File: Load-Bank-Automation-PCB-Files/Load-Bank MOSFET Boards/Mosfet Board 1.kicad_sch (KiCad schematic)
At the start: 21 parts, among them J1 Conn_02x03_Counter_Clockwise, J24 PHNX_CONN_1017521, Q22 GSGN0648, Q3 GSGN0648, U10 MCP6006-OTVAO, U7 ACS711xLCTR-25AB, U8 IRS10752LPBF

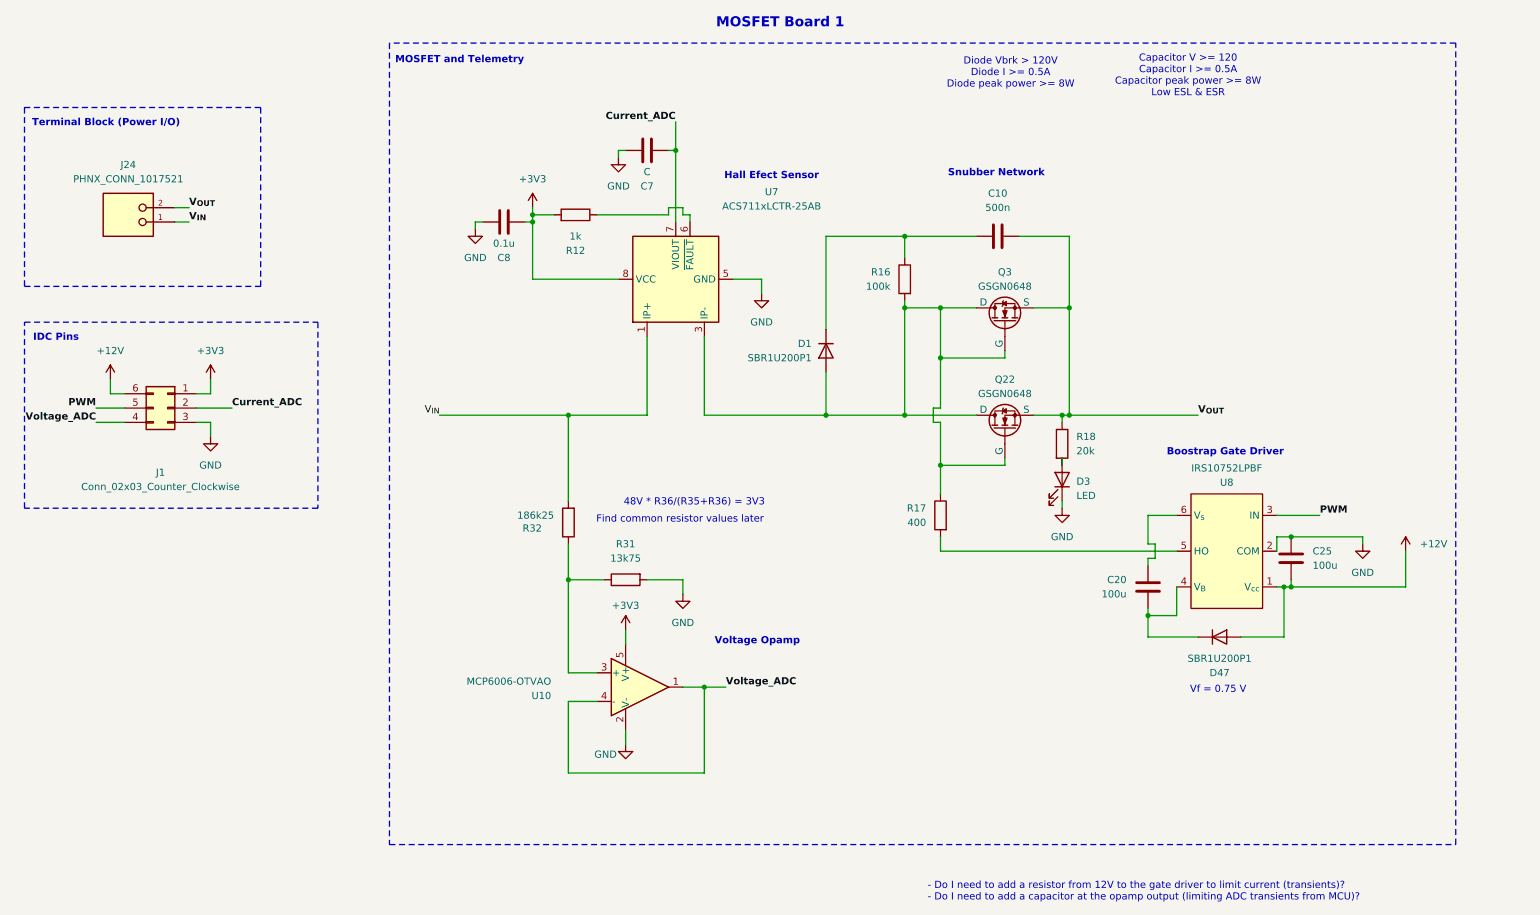
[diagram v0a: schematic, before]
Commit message: Almost completed MOSFET board component selection
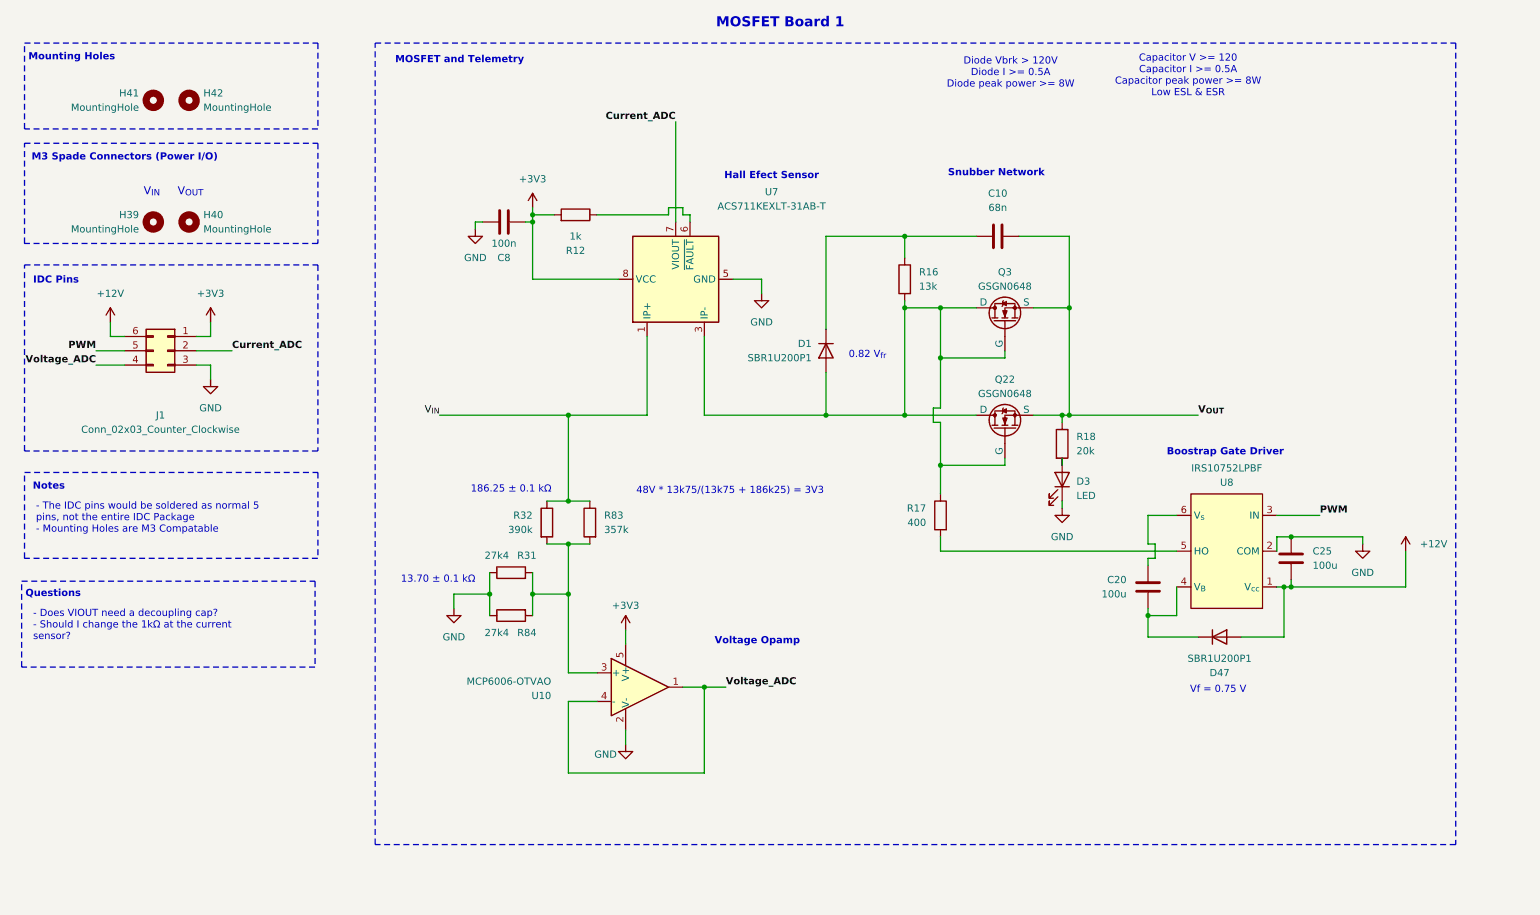
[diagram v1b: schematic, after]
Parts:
- removed C7: C, Capacitor_SMD:C_0603_1608Metric_Pad1.08x0.95mm_HandSolder, symbol Device:C
- removed J24: PHNX_CONN_1017521, ecocad_lib_footprints:PHOENIX_1017521, symbol EcoCar_Library:PHNX_CONN_1017521
- added H39, H40, H41, H42: MountingHole, TerminalBlock_MetzConnect:TerminalBlock_MetzConnect_360271_1x01_Horizontal_ScrewM3.0_Boxed, symbol Mechanical:MountingHole
- added R83: 357k, Resistor_SMD:R_1206_3216Metric_Pad1.30x1.75mm_HandSolder, symbol Device:R
- added R84: 27k4, Resistor_SMD:R_1206_3216Metric_Pad1.30x1.75mm_HandSolder, symbol Device:R
- C10: value 500n -> 68n; footprint (none) -> Capacitor_SMD:C_1206_3216Metric_Pad1.33x1.80mm_HandSolder
- C8: value 0.1u -> 100n
- R16: value 100k -> 13k; footprint (none) -> Resistor_THT:R_Axial_DIN0204_L3.6mm_D1.6mm_P7.62mm_Horizontal
- R31: value 13k75 -> 27k4; footprint (none) -> Resistor_SMD:R_1206_3216Metric_Pad1.30x1.75mm_HandSolder
- R32: value 186k25 -> 390k; footprint (none) -> Resistor_SMD:R_1206_3216Metric_Pad1.30x1.75mm_HandSolder
- U7: value ACS711xLCTR-25AB -> ACS711KEXLT-31AB-T; footprint Package_SO:SOIC-8_3.9x4.9mm_P1.27mm -> Package_DFN_QFN:XDCR_ACS711KEXLT-15AB-T
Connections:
- net GND: now also R31.1, R84.1; no longer R31.2
- net V_{IN}: now also R32.1, R83.1; no longer R32.2
- new net: R31.2, R32.2, R83.2, R84.2, U10.3 (+)
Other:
- note added: "- Does VIOUT need a decoupling cap? - Should I change the 1kΩ at the current sensor?"
- note added: "- The IDC pins would be soldered as normal 5 pins, not the entire IDC Package - Mounting Holes are M3 Compatable"
- note added: "0.82 V_{fr}"
- note added: "13.70 ± 0.1 kΩ"
- note added: "186.25 ± 0.1 kΩ"
- note added: "48V * 13k75/(13k75 + 186k25) = 3V3"
- note added: "M3 Spade Connectors (Power I/O)"
- note added: "Mounting Holes"
- note added: "Notes"
- note added: "Questions"
- note added: "V_{IN}"
- note added: "V_{OUT}"
- note removed: "- Do I need to add a resistor from 12V to the gate driver to limit current (transients)? - Do I need to add a capacitor at the opamp output (limiting ADC transients from MCU)?"
- note removed: "48V * R36/(R35+R36) = 3V3"
- note removed: "Find common resistor values later"
- note removed: "Terminal Block (Power I/O)"
- moved on the sheet: J1

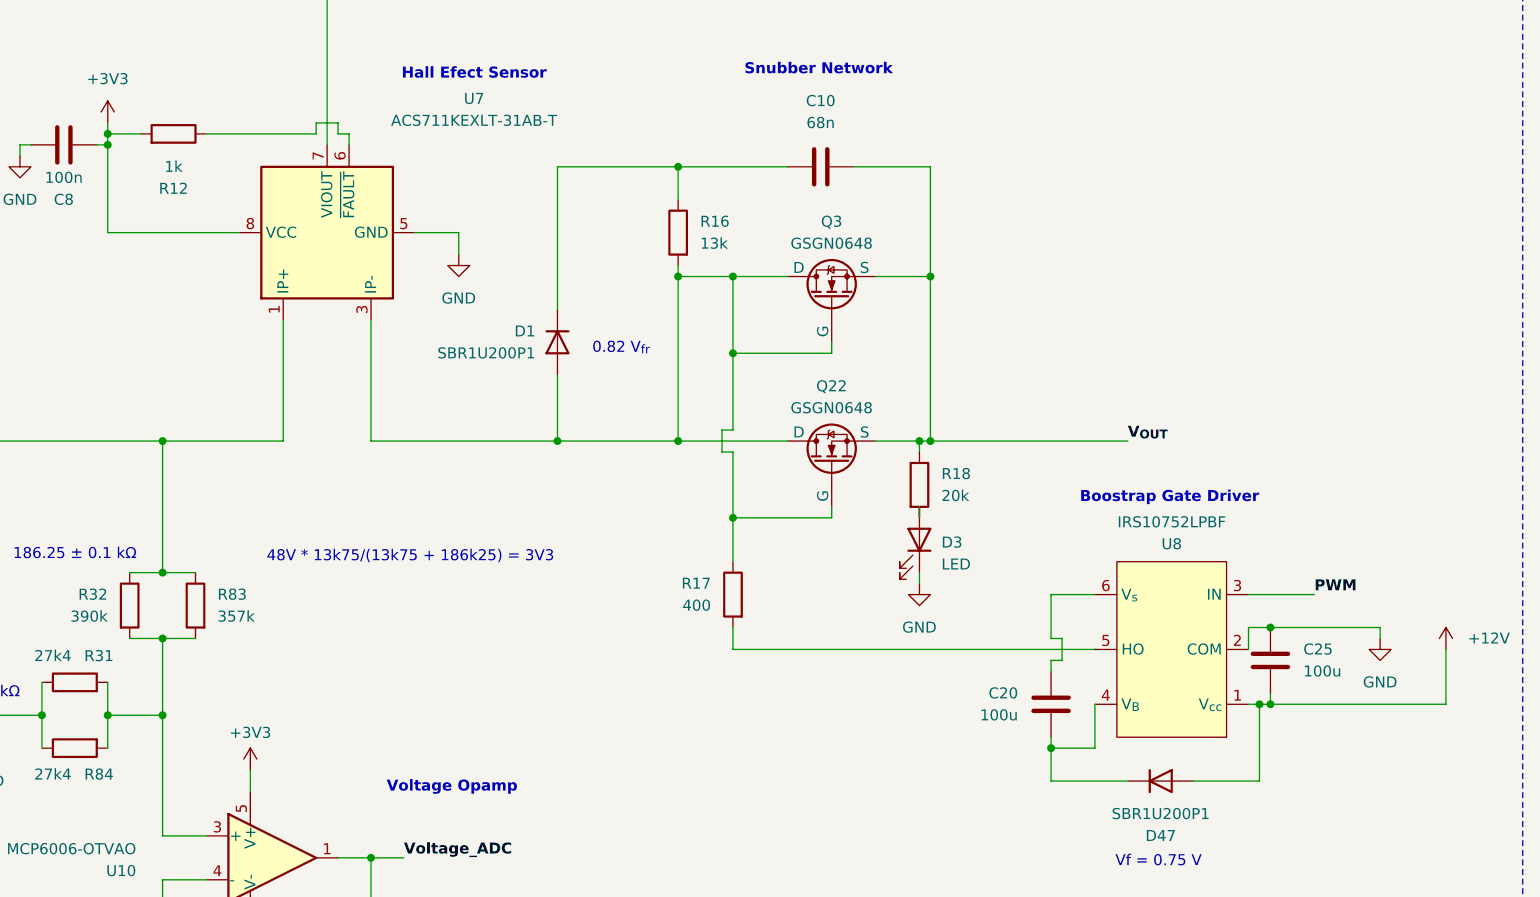
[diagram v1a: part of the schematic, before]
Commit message: All footprints assigned and new schematic changes
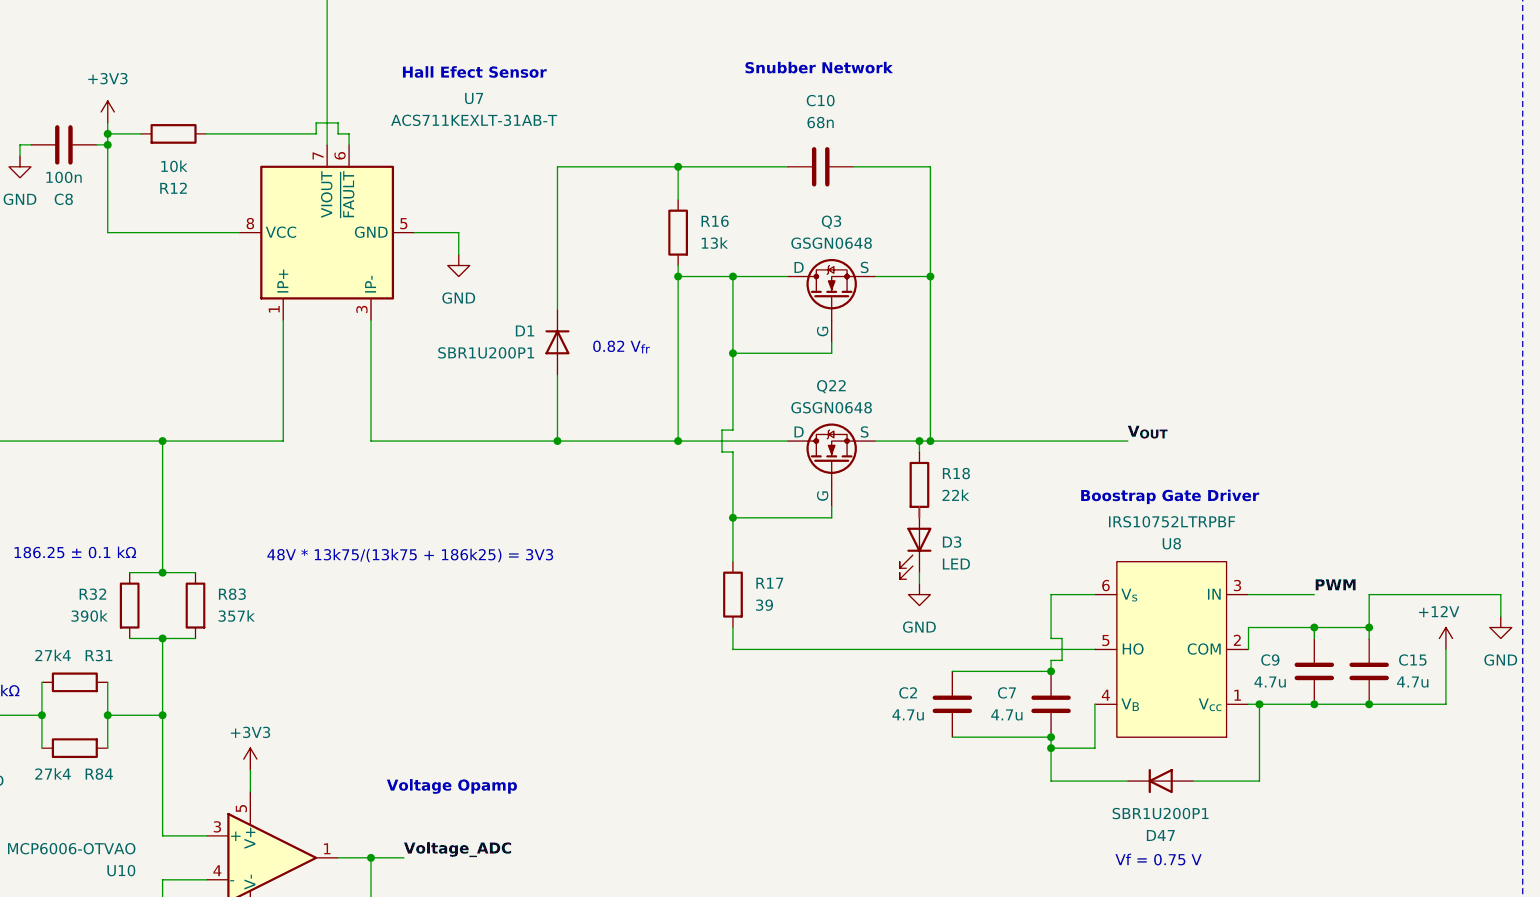
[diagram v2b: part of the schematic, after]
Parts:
- removed C20, C25: 100u, Capacitor_SMD:C_0603_1608Metric_Pad1.08x0.95mm_HandSolder, symbol Device:C
- added C15, C2, C7, C9: 4.7u, Capacitor_SMD:C_1210_3225Metric_Pad1.33x2.70mm_HandSolder, symbol Device:C
- C8: footprint Capacitor_SMD:C_0603_1608Metric_Pad1.08x0.95mm_HandSolder -> Capacitor_SMD:C_1206_3216Metric_Pad1.33x1.80mm_HandSolder
- R12: value 1k -> 10k; footprint (none) -> Resistor_SMD:R_1206_3216Metric_Pad1.30x1.75mm_HandSolder
- R17: value 400 -> 39; footprint (none) -> Resistor_SMD:R_1206_3216Metric_Pad1.30x1.75mm_HandSolder
- R18: value 20k -> 22k; footprint (none) -> Resistor_SMD:R_1206_3216Metric_Pad1.30x1.75mm_HandSolder
- U8: value IRS10752LPBF -> IRS10752LTRPBF
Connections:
- net +12V: now also C15.1, C9.1
- net GND: now also C15.2, C9.2
- net at U8.6 (V_{s}): now also C2.2, C7.2
- net at D47.1 (K), U8.4 (V_{B}): now also C2.1, C7.1

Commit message: A
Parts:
- removed J1: Conn_02x03_Counter_Clockwise, Connector_IDC:IDC-Header_2x03_P2.54mm_Vertical, symbol Connector_Generic:Conn_02x03_Counter_Clockwise
- added J2, J22: Conn_01x03, Connector_PinHeader_1.00mm:IDC_PinHeader_1x03_P1.00mm_Vertical, symbol Connector_Generic:Conn_01x03
- H41, H42: footprint TerminalBlock_MetzConnect:TerminalBlock_MetzConnect_360271_1x01_Horizontal_ScrewM3.0_Boxed -> MountingHole:MountingHole_3.2mm_M3
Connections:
- net +12V: now also J22.3 (Pin_3)
- net +3V3: now also J22.2 (Pin_2)
- net Current_ADC: now also J2.3 (Pin_3)
- net GND: now also J22.1 (Pin_1)
- net PWM: now also J2.1 (Pin_1)
- net Voltage_ADC: now also J2.2 (Pin_2)

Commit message: A
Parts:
- removed C15, C9: 4.7u, Capacitor_SMD:C_1210_3225Metric_Pad1.33x2.70mm_HandSolder, symbol Device:C
- C2: value 4.7u -> 100n; footprint Capacitor_SMD:C_1210_3225Metric_Pad1.33x2.70mm_HandSolder -> Capacitor_SMD:C_0603_1608Metric_Pad1.08x0.95mm_HandSolder
- D1, D47: footprint Diode_SMD:D_PowerDI-123 -> Diode_SMD:D_SMB_Handsoldering
- R18: value 22k -> 20k
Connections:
- net +12V: now also C2.2
- net GND: now also C2.1
- net at C7.1, D47.1 (K), U8.4 (V_{B}): no longer C2.1
- net at C7.2, U8.6 (V_{s}): no longer C2.2
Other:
- note added: "0.59 V_{fr}"
- note removed: "0.82 V_{fr}"
- note removed: "Vf = 0.75 V"

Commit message: A
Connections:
- net +3V3: now also U7.12 (VCC); no longer U7.8 (VCC)
- net Current_ADC: now also U7.11 (VIOUT); no longer U7.7 (VIOUT)
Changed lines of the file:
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@@
 			)
 		)
-		(property "Datasheet" "https://www.digikey.com/en/products/detail/allegro-microsystems/ACS711KEXLT-31AB-T/3868195"
+		(property "Datasheet" "http://www.allegromicro.com/~/Media/Files/Datasheets/ACS711-Datasheet.ashx"
 			(at 134.62 62.23 0)
 			(effects
@@
 		(pin "1"
 		)
-		(pin "8"
+		(pin "12"
 		)
 		(pin "5"
 		)
-		(pin "7"
+		(pin "11"
 		)
 		(pin "6"
